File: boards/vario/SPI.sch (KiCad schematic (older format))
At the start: 8 parts

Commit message: PS/2 schematic
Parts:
- gave numbers to parts that had none: 6
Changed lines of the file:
@@
 $Descr A3 16535 11693
 encoding utf-8
-Sheet 2 2
+Sheet 2 3
 Title "SPI controller"
 Date "2020-12-23"
@@
 P 4650 3150
 AR Path="/5FE61758" Ref="U?"  Part="1"
-AR Path="/5FE5ABE2/5FE61758" Ref="U?"  Part="1"
-F 0 "U?" H 5050 2600 50  0000 C CNN
+AR Path="/5FE5ABE2/5FE61758" Ref="U1"  Part="1"
+F 0 "U1" H 5050 2600 50  0000 C CNN
 F 1 "74HC273" H 5050 2450 50  0000 C CNN
 F 2 "" H 4650 3150 50  0001 C CNN
@@
 P 4650 3950
 AR Path="/5FE6176E" Ref="#PWR?"  Part="1"
-AR Path="/5FE5ABE2/5FE6176E" Ref="#PWR?"  Part="1"
-F 0 "#PWR?" H 4650 3700 50  0001 C CNN
+AR Path="/5FE5ABE2/5FE6176E" Ref="#PWR09"  Part="1"
+F 0 "#PWR09" H 4650 3700 50  0001 C CNN
 F 1 "GND" V 4655 3822 50  0000 R CNN
 F 2 "" H 4650 3950 50  0001 C CNN
@@
 P 4650 2350
 AR Path="/5FE61774" Ref="#PWR?"  Part="1"
-AR Path="/5FE5ABE2/5FE61774" Ref="#PWR?"  Part="1"
-F 0 "#PWR?" H 4650 2200 50  0001 C CNN
+AR Path="/5FE5ABE2/5FE61774" Ref="#PWR08"  Part="1"
+F 0 "#PWR08" H 4650 2200 50  0001 C CNN
 F 1 "VCC" V 4665 2478 50  0000 L CNN
 F 2 "" H 4650 2350 50  0001 C CNN
@@
 P 7350 3200
 AR Path="/5FE6177B" Ref="U?"  Part="1"
-AR Path="/5FE5ABE2/5FE6177B" Ref="U?"  Part="1"
-F 0 "U?" H 7750 2450 50  0000 C CNN
+AR Path="/5FE5ABE2/5FE6177B" Ref="U5"  Part="1"
+F 0 "U5" H 7750 2450 50  0000 C CNN
 F 1 "74LS151" H 7750 2300 50  0000 C CNN
 F 2 "" H 7350 3200 50  0001 C CNN
@@
 P 7350 2300
 AR Path="/5FE61789" Ref="#PWR?"  Part="1"
-AR Path="/5FE5ABE2/5FE61789" Ref="#PWR?"  Part="1"
-F 0 "#PWR?" H 7350 2150 50  0001 C CNN
+AR Path="/5FE5ABE2/5FE61789" Ref="#PWR019"  Part="1"
+F 0 "#PWR019" H 7350 2150 50  0001 C CNN
 F 1 "VCC" V 7365 2428 50  0000 L CNN
 F 2 "" H 7350 2300 50  0001 C CNN
@@
 P 7350 4200
 AR Path="/5FE6178F" Ref="#PWR?"  Part="1"
-AR Path="/5FE5ABE2/5FE6178F" Ref="#PWR?"  Part="1"
-F 0 "#PWR?" H 7350 3950 50  0001 C CNN
+AR Path="/5FE5ABE2/5FE6178F" Ref="#PWR020"  Part="1"
+F 0 "#PWR020" H 7350 3950 50  0001 C CNN
 F 1 "GND" V 7355 4072 50  0000 R CNN
 F 2 "" H 7350 4200 50  0001 C CNN
@@
 P 6850 3900
 AR Path="/5FE6179A" Ref="#PWR?"  Part="1"
-AR Path="/5FE5ABE2/5FE6179A" Ref="#PWR?"  Part="1"
-F 0 "#PWR?" H 6850 3650 50  0001 C CNN
+AR Path="/5FE5ABE2/5FE6179A" Ref="#PWR016"  Part="1"
+F 0 "#PWR016" H 6850 3650 50  0001 C CNN
 F 1 "GND" V 6855 3772 50  0000 R CNN
 F 2 "" H 6850 3900 50  0001 C CNN
@@
 P 4650 5600
 AR Path="/5FE617A0" Ref="U?"  Part="1"
-AR Path="/5FE5ABE2/5FE617A0" Ref="U?"  Part="1"
-F 0 "U?" H 5100 5050 50  0000 C CNN
+AR Path="/5FE5ABE2/5FE617A0" Ref="U2"  Part="1"
+F 0 "U2" H 5100 5050 50  0000 C CNN
 F 1 "74LS161" H 5000 4950 50  0000 C CNN
 F 2 "" H 4650 5600 50  0001 C CNN
@@
 P 4650 6400
 AR Path="/5FE617AA" Ref="#PWR?"  Part="1"
-AR Path="/5FE5ABE2/5FE617AA" Ref="#PWR?"  Part="1"
-F 0 "#PWR?" H 4650 6150 50  0001 C CNN
+AR Path="/5FE5ABE2/5FE617AA" Ref="#PWR011"  Part="1"
+F 0 "#PWR011" H 4650 6150 50  0001 C CNN
 F 1 "GND" V 4655 6272 50  0000 R CNN
 F 2 "" H 4650 6400 50  0001 C CNN
@@
 P 4650 4800
 AR Path="/5FE617B0" Ref="#PWR?"  Part="1"
-AR Path="/5FE5ABE2/5FE617B0" Ref="#PWR?"  Part="1"
-F 0 "#PWR?" H 4650 4650 50  0001 C CNN
+AR Path="/5FE5ABE2/5FE617B0" Ref="#PWR010"  Part="1"
+F 0 "#PWR010" H 4650 4650 50  0001 C CNN
 F 1 "VCC" V 4665 4928 50  0000 L CNN
 F 2 "" H 4650 4800 50  0001 C CNN
@@
 P 4150 5000
 AR Path="/5FE617B6" Ref="#PWR?"  Part="1"
-AR Path="/5FE5ABE2/5FE617B6" Ref="#PWR?"  Part="1"
-F 0 "#PWR?" H 4150 4850 50  0001 C CNN
+AR Path="/5FE5ABE2/5FE617B6" Ref="#PWR06"  Part="1"
+F 0 "#PWR06" H 4150 4850 50  0001 C CNN
 F 1 "VCC" V 4165 5128 50  0000 L CNN
 F 2 "" H 4150 5000 50  0001 C CNN
@@
 P 4100 5700
 AR Path="/5FE617C3" Ref="#PWR?"  Part="1"
-AR Path="/5FE5ABE2/5FE617C3" Ref="#PWR?"  Part="1"
-F 0 "#PWR?" H 4100 5550 50  0001 C CNN
+AR Path="/5FE5ABE2/5FE617C3" Ref="#PWR05"  Part="1"
+F 0 "#PWR05" H 4100 5550 50  0001 C CNN
 F 1 "VCC" V 4115 5828 50  0000 L CNN
 F 2 "" H 4100 5700 50  0001 C CNN
@@
 P 7300 5600
 AR Path="/5FE62655" Ref="U?"  Part="1"
-AR Path="/5FE5ABE2/5FE62655" Ref="U?"  Part="1"
-F 0 "U?" H 7700 5050 50  0000 C CNN
+AR Path="/5FE5ABE2/5FE62655" Ref="U4"  Part="1"
+F 0 "U4" H 7700 5050 50  0000 C CNN
 F 1 "74HC273" H 7700 4900 50  0000 C CNN
 F 2 "" H 7300 5600 50  0001 C CNN
@@
 P 7300 6400
 AR Path="/5FE66867" Ref="#PWR?"  Part="1"
-AR Path="/5FE5ABE2/5FE66867" Ref="#PWR?"  Part="1"
-F 0 "#PWR?" H 7300 6150 50  0001 C CNN
+AR Path="/5FE5ABE2/5FE66867" Ref="#PWR018"  Part="1"
+F 0 "#PWR018" H 7300 6150 50  0001 C CNN
 F 1 "GND" V 7305 6272 50  0000 R CNN
 F 2 "" H 7300 6400 50  0001 C CNN
@@
 P 7300 4800
 AR Path="/5FE66E39" Ref="#PWR?"  Part="1"
-AR Path="/5FE5ABE2/5FE66E39" Ref="#PWR?"  Part="1"
-F 0 "#PWR?" H 7300 4650 50  0001 C CNN
+AR Path="/5FE5ABE2/5FE66E39" Ref="#PWR017"  Part="1"
+F 0 "#PWR017" H 7300 4650 50  0001 C CNN
 F 1 "VCC" V 7315 4928 50  0000 L CNN
 F 2 "" H 7300 4800 50  0001 C CNN
@@
 clk
 $Comp
-L 74xx:74HC244 U?
+L 74xx:74HC244 U6
 U 1 1 5FE6C343
 P 9150 5600
-F 0 "U?" H 9600 4950 50  0000 C CNN
+F 0 "U6" H 9600 4950 50  0000 C CNN
 F 1 "74HC244" H 9600 4850 50  0000 C CNN
 F 2 "" H 9150 5600 50  0001 C CNN
@@
 P 9150 6400
 AR Path="/5FE7030B" Ref="#PWR?"  Part="1"
-AR Path="/5FE5ABE2/5FE7030B" Ref="#PWR?"  Part="1"
-F 0 "#PWR?" H 9150 6150 50  0001 C CNN
+AR Path="/5FE5ABE2/5FE7030B" Ref="#PWR022"  Part="1"
+F 0 "#PWR022" H 9150 6150 50  0001 C CNN
 F 1 "GND" V 9155 6272 50  0000 R CNN
 F 2 "" H 9150 6400 50  0001 C CNN
@@
 P 9150 4800
 AR Path="/5FE709A9" Ref="#PWR?"  Part="1"
-AR Path="/5FE5ABE2/5FE709A9" Ref="#PWR?"  Part="1"
-F 0 "#PWR?" H 9150 4650 50  0001 C CNN
+AR Path="/5FE5ABE2/5FE709A9" Ref="#PWR021"  Part="1"
+F 0 "#PWR021" H 9150 4650 50  0001 C CNN
 F 1 "VCC" V 9165 4928 50  0000 L CNN
 F 2 "" H 9150 4800 50  0001 C CNN
@@
 $EndComp
 $Comp
-L 74xx:74HC74 U?
+L 74xx:74HC74 U3
 U 1 1 5FE7AD90
 P 4650 7600
-F 0 "U?" H 5000 7400 50  0000 C CNN
+F 0 "U3" H 5000 7400 50  0000 C CNN
 F 1 "74HC74" H 5050 7300 50  0000 C CNN
 F 2 "" H 4650 7600 50  0001 C CNN
@@
 $EndComp
 $Comp
-L 74xx:74HC74 U?
+L 74xx:74HC74 U3
 U 2 1 5FE7C18A
 P 6650 7600
-F 0 "U?" H 6950 7350 50  0000 C CNN
+F 0 "U3" H 6950 7350 50  0000 C CNN
 F 1 "74HC74" H 6950 7250 50  0000 C CNN
 F 2 "" H 6650 7600 50  0001 C CNN
@@
 $EndComp
 $Comp
-L 74xx:74HC74 U?
+L 74xx:74HC74 U3
 U 3 1 5FE7C9F6
 P 5450 9400
-F 0 "U?" H 5680 9446 50  0000 L CNN
+F 0 "U3" H 5680 9446 50  0000 L CNN
 F 1 "74HC74" H 5680 9355 50  0000 L CNN
 F 2 "" H 5450 9400 50  0001 C CNN
@@
 P 5450 9800
 AR Path="/5FE7D6EE" Ref="#PWR?"  Part="1"
-AR Path="/5FE5ABE2/5FE7D6EE" Ref="#PWR?"  Part="1"
-F 0 "#PWR?" H 5450 9550 50  0001 C CNN
+AR Path="/5FE5ABE2/5FE7D6EE" Ref="#PWR014"  Part="1"
+F 0 "#PWR014" H 5450 9550 50  0001 C CNN
 F 1 "GND" V 5455 9672 50  0000 R CNN
 F 2 "" H 5450 9800 50  0001 C CNN
@@
 P 5450 9000
 AR Path="/5FE7DD29" Ref="#PWR?"  Part="1"
-AR Path="/5FE5ABE2/5FE7DD29" Ref="#PWR?"  Part="1"
-F 0 "#PWR?" H 5450 8850 50  0001 C CNN
+AR Path="/5FE5ABE2/5FE7DD29" Ref="#PWR013"  Part="1"
+F 0 "#PWR013" H 5450 8850 50  0001 C CNN
 F 1 "VCC" V 5465 9128 50  0000 L CNN
 F 2 "" H 5450 9000 50  0001 C CNN
@@
 P 4350 7500
 AR Path="/5FE7FC4F" Ref="#PWR?"  Part="1"
-AR Path="/5FE5ABE2/5FE7FC4F" Ref="#PWR?"  Part="1"
-F 0 "#PWR?" H 4350 7350 50  0001 C CNN
+AR Path="/5FE5ABE2/5FE7FC4F" Ref="#PWR07"  Part="1"
+F 0 "#PWR07" H 4350 7350 50  0001 C CNN
 F 1 "VCC" V 4365 7628 50  0000 L CNN
 F 2 "" H 4350 7500 50  0001 C CNN
@@
 P 4650 7300
 AR Path="/5FE80BC0" Ref="#PWR?"  Part="1"
-AR Path="/5FE5ABE2/5FE80BC0" Ref="#PWR?"  Part="1"
-F 0 "#PWR?" H 4650 7150 50  0001 C CNN
+AR Path="/5FE5ABE2/5FE80BC0" Ref="#PWR012"  Part="1"
+F 0 "#PWR012" H 4650 7150 50  0001 C CNN
 F 1 "VCC" V 4665 7428 50  0000 L CNN
 F 2 "" H 4650 7300 50  0001 C CNN
@@
 P 6650 7300
 AR Path="/5FE83B74" Ref="#PWR?"  Part="1"
-AR Path="/5FE5ABE2/5FE83B74" Ref="#PWR?"  Part="1"
-F 0 "#PWR?" H 6650 7150 50  0001 C CNN
+AR Path="/5FE5ABE2/5FE83B74" Ref="#PWR015"  Part="1"
+F 0 "#PWR015" H 6650 7150 50  0001 C CNN
 F 1 "VCC" V 6665 7428 50  0000 L CNN
 F 2 "" H 6650 7300 50  0001 C CNN
@@
 Text Label 1250 2050 0    50   ~ 0
 d[0..7]
-Text HLabel 1200 2350 0    50   Input ~ 0
-~rst
 Text Label 1200 2350 0    50   ~ 0
 ~rst
@@
 Text Label 11300 3000 2    50   ~ 0
 rdy
+Text GLabel 1200 2350 0    50   Input ~ 0
+~rst
+Wire Bus Line
+	1250 2050 1700 2050
+Entry Wire Line
+	1800 2450 1700 2350
+Entry Wire Line
+	1800 2550 1700 2450
+Entry Wire Line
+	1800 2650 1700 2550
+Entry Wire Line
+	1800 2750 1700 2650
+Entry Wire Line
+	1800 2850 1700 2750
+Entry Wire Line
+	1800 2950 1700 2850
+Entry Wire Line
+	1800 3050 1700 2950
+Entry Wire Line
+	1800 3150 1700 3050
+Text Label 2000 3150 0    50   ~ 0
+d7
+Text Label 2000 3050 0    50   ~ 0
+d6
+Text Label 2000 2950 0    50   ~ 0
+d5
+Text Label 2000 2850 0    50   ~ 0
+d4
+Text Label 2000 2750 0    50   ~ 0
+d3
+Text Label 2000 2650 0    50   ~ 0
+d2
+Text Label 2000 2550 0    50   ~ 0
+d1
+Text Label 2000 2450 0    50   ~ 0
+d0
+Wire Wire Line
+	1800 2450 2000 2450
+Wire Wire Line
+	2000 2550 1800 2550
+Wire Wire Line
+	1800 2650 2000 2650
+Wire Wire Line
+	2000 2750 1800 2750
+Wire Wire Line
+	1800 2850 2000 2850
+Wire Wire Line
+	2000 2950 1800 2950
+Wire Wire Line
+	1800 3050 2000 3050
+Wire Wire Line
+	2000 3150 1800 3150
+Wire Bus Line
+	1700 2050 1700 3050
 $EndSCHEMATC

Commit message: SPI: some capacitors
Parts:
- added C27, C28, C29, C30, C31, C32: 0.1, symbol Device:C
- added Q4: Q_PMOS_DGS, symbol Device:Q_PMOS_DGS
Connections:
- net GND: now also C27.2, C28.2, C29.2, C30.2, C31.2, C32.2
- net VCC: now also C27.1, C28.1, C29.1, C30.1, C31.1, C32.1, Q4.3 (S)
- net rdy: now also Q4.2 (G)
- new net ~rdy: Q4.1 (D)

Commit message: SPI: implement missing logic
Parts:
- added C33: C, symbol Device:C
- added C34, C35, C36: 0.1, symbol Device:C
- added R5: R, symbol Device:R
- added U31: 74LS14, symbol 74xx:74LS14
- added U32: 74LS32, symbol 74xx:74LS32
- added U33: 74LS08, symbol 74xx:74LS08
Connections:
- net GND: now also C33.2, C34.2, C35.2, C36.2, U31.7 (GND), U32.7 (GND), U33.4, U33.5, U33.7 (GND)
- net VCC: now also C34.1, C35.1, C36.1, U31.14 (VCC), U32.14 (VCC), U33.12, U33.13, U33.14 (VCC)
- net clk: now also U31.8
- net count3: now also U31.5
- net rdy: now also U32.8
- net rdy_int: now also U32.9
- net reg_send_cp: now also U32.3
- net ~clk: now also U31.9, U32.6
- net ~int_clk: now also U31.4, U32.4
- net ~int_rst: now also U33.3
- net ~oe: now also U32.12
- net ~oe_to_d: now also U32.11
- net ~rst: now also U33.1
- net ~sel: now also U32.1, U32.10, U32.13
- net ~we: now also U32.2
- net ~clk_ena: now reaches U3.8 (~Q)
- net ~clk_ena: now also U32.5
- new net: C33.1, R5.2, U31.1
- new net: U33.10, U33.11, U33.9
- new net int_clk: R5.1, U31.2, U31.3
- new net ~count3: U31.6, U33.2
- no-connect marks 3 -> 5
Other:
- note added: "SPI clock, ~~1 MHz"
- moved on the sheet: C27, C28, C29, C30, C31, C32, U1, U2, U3A, U3B, U3C, U4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

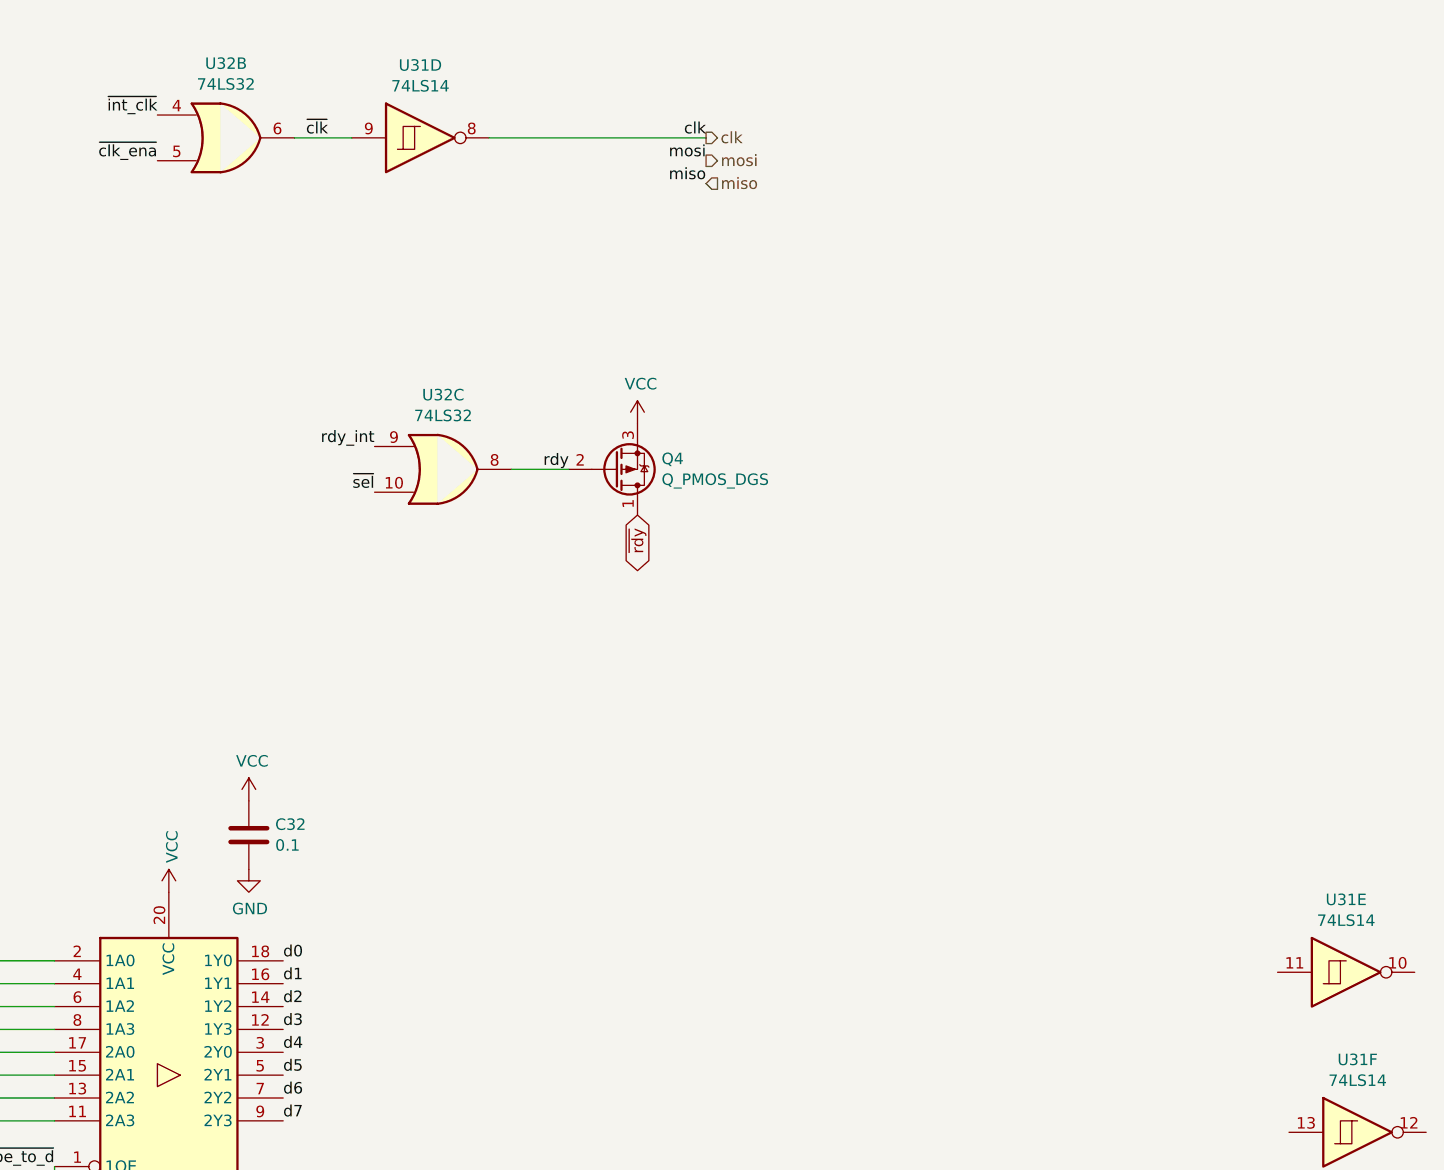
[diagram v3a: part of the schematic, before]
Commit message: Vario: memory card connection and power
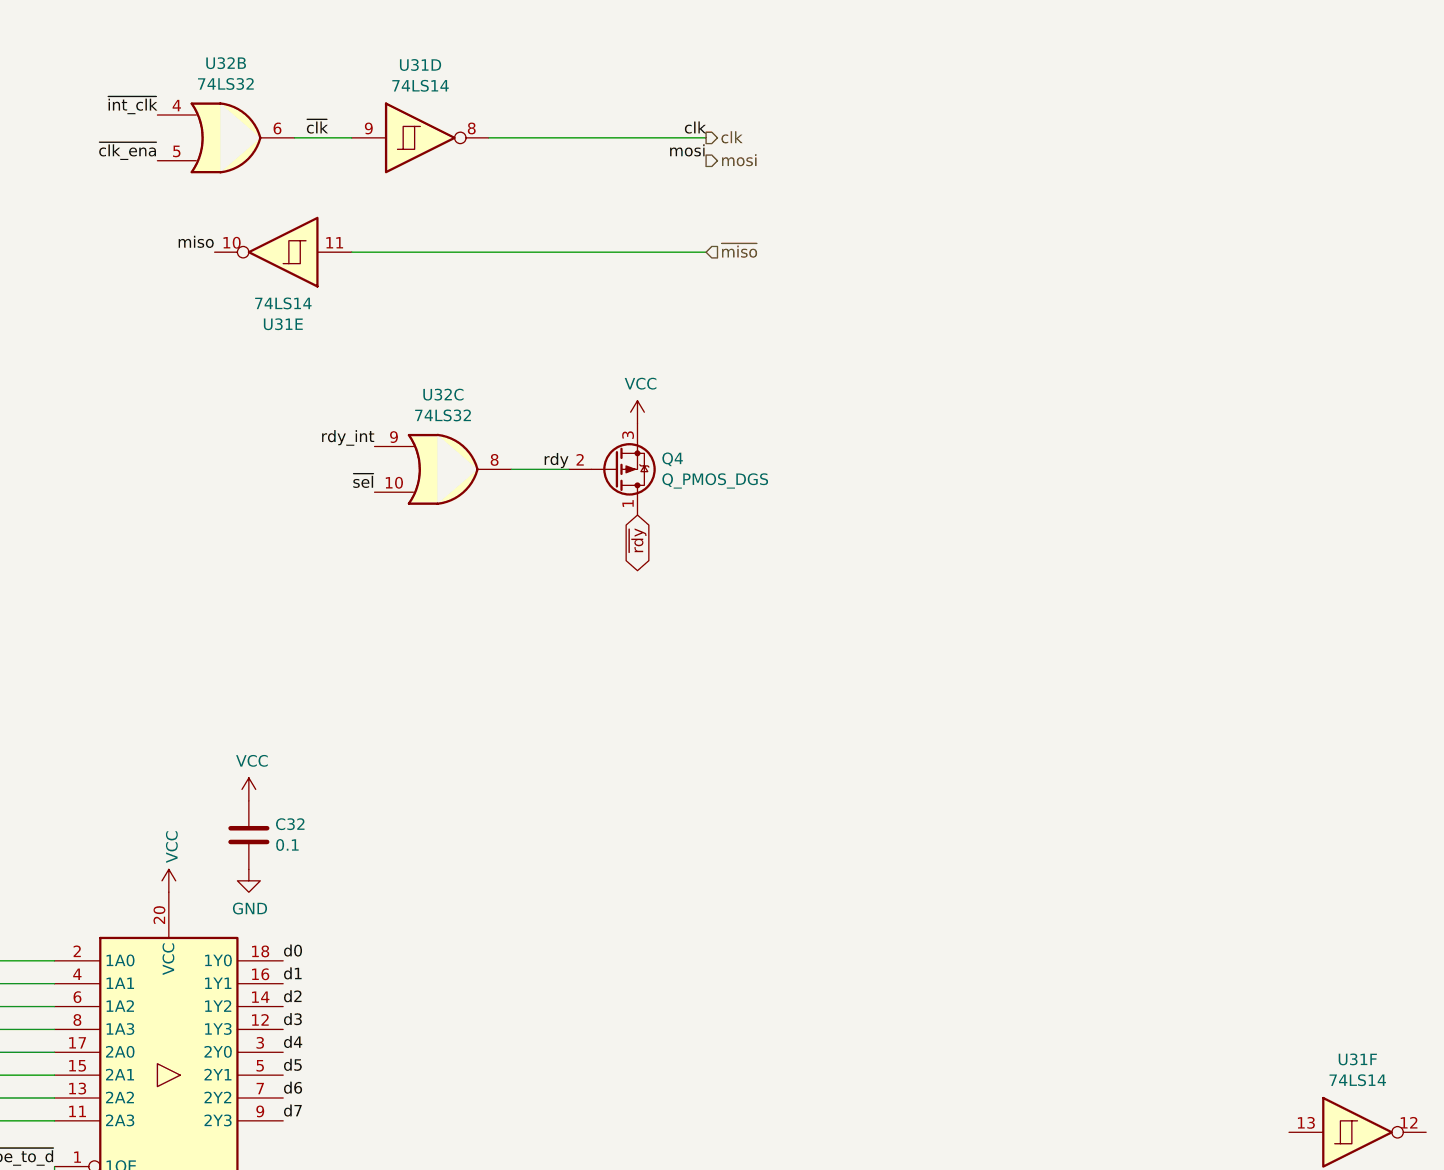
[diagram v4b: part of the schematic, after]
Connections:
- net miso: now also U31.10
- net ~miso: now reaches U31.11
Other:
- moved on the sheet: U31E
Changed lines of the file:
@@
 Text HLabel 11300 2600 2    50   Output ~ 0
 mosi
-Text HLabel 11300 2700 2    50   Input ~ 0
-miso
+Text HLabel 11300 3000 2    50   Input ~ 0
+~miso
 Text Label 11300 2600 2    50   ~ 0
 mosi
 Text Label 11300 2500 2    50   ~ 0
 clk
-Text Label 11300 2700 2    50   ~ 0
+Text Label 9150 3000 2    50   ~ 0
 miso
 Text HLabel 1250 2050 0    50   BiDi ~ 0
@@
 L 74xx:74LS14 U31
 U 5 1 5FEBABC1
-P 14100 6150
-F 0 "U31" H 14100 6467 50  0000 C CNN
-F 1 "74LS14" H 14100 6376 50  0000 C CNN
-F 2 "" H 14100 6150 50  0001 C CNN
-F 3 "http://www.ti.com/lit/gpn/sn74LS14" H 14100 6150 50  0001 C CNN
-	5    14100 6150
-	1    0    0    -1
+P 9450 3000
+F 0 "U31" H 9450 3317 50  0000 C CNN
+F 1 "74LS14" H 9450 3226 50  0000 C CNN
+F 2 "" H 9450 3000 50  0001 C CNN
+F 3 "http://www.ti.com/lit/gpn/sn74LS14" H 9450 3000 50  0001 C CNN
+	5    9450 3000
+	-1   0    0    1
 $EndComp
 $Comp
@@
 NoConn ~ 13750 8850
 NoConn ~ 6750 8500
+Wire Wire Line
+	11300 3000 9750 3000
 Wire Bus Line
 	1700 2050 1700 3050
